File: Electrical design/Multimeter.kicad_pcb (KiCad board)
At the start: 2 copper layers, 191.5 x 133 mm, 191 parts, among them P101 CONN_02X07, P102 CONN_01X06, P201 10 A, P202 mA, P203 V R, P204 COMMON, P401 CONN_01X01, P402 CONN_01X01, P403 CONN_01X01, P404 CONN_01X01, P405 CONN_01X01, P406 CONN_01X05, P407 CONN_01X05, P501 USB_OTG, Q101 Q_PMOS_GSD, Q102 Q_NMOS_GSD, Q201 Q_NMOS_GSD, Q301 Q_PMOS_GSD, Q302 Q_NMOS_GSD, Q501 Q_NMOS_GSD, Q502 Q_PMOS_GSD, SW401 SW_PUSH, U101 STM32F373R8Tx, U102 ILI9341_LCD_Breakout, U103 BD4835, U201 CT138, U202 MCP6002, U203 MCP6N11, U204 74LVC1G66 GNDA, U205 CT138, U206 74LVC1G66 GNDA, U207 TSV634, U208 74LVC1G66 GNDA, U209 74LVC1G66 GNDA, U210 74LVC1G66 GNDA, U211 74LVC1G66 GNDA, U212 74LVC1G66 GNDA, U213 74LVC1G66 GNDA, U214 74LVC1G66 GNDA, U215 74LVC1G66 GNDA, U216 74LVC1G66 GNDA, U217 74LVC1G66 GNDA, U218 74LVC1G66 GNDA, U301 NCV551SN33T1G, U302 MAX6070, U501 TPD2E001, U502 MCP73834, Y101 8 MHz

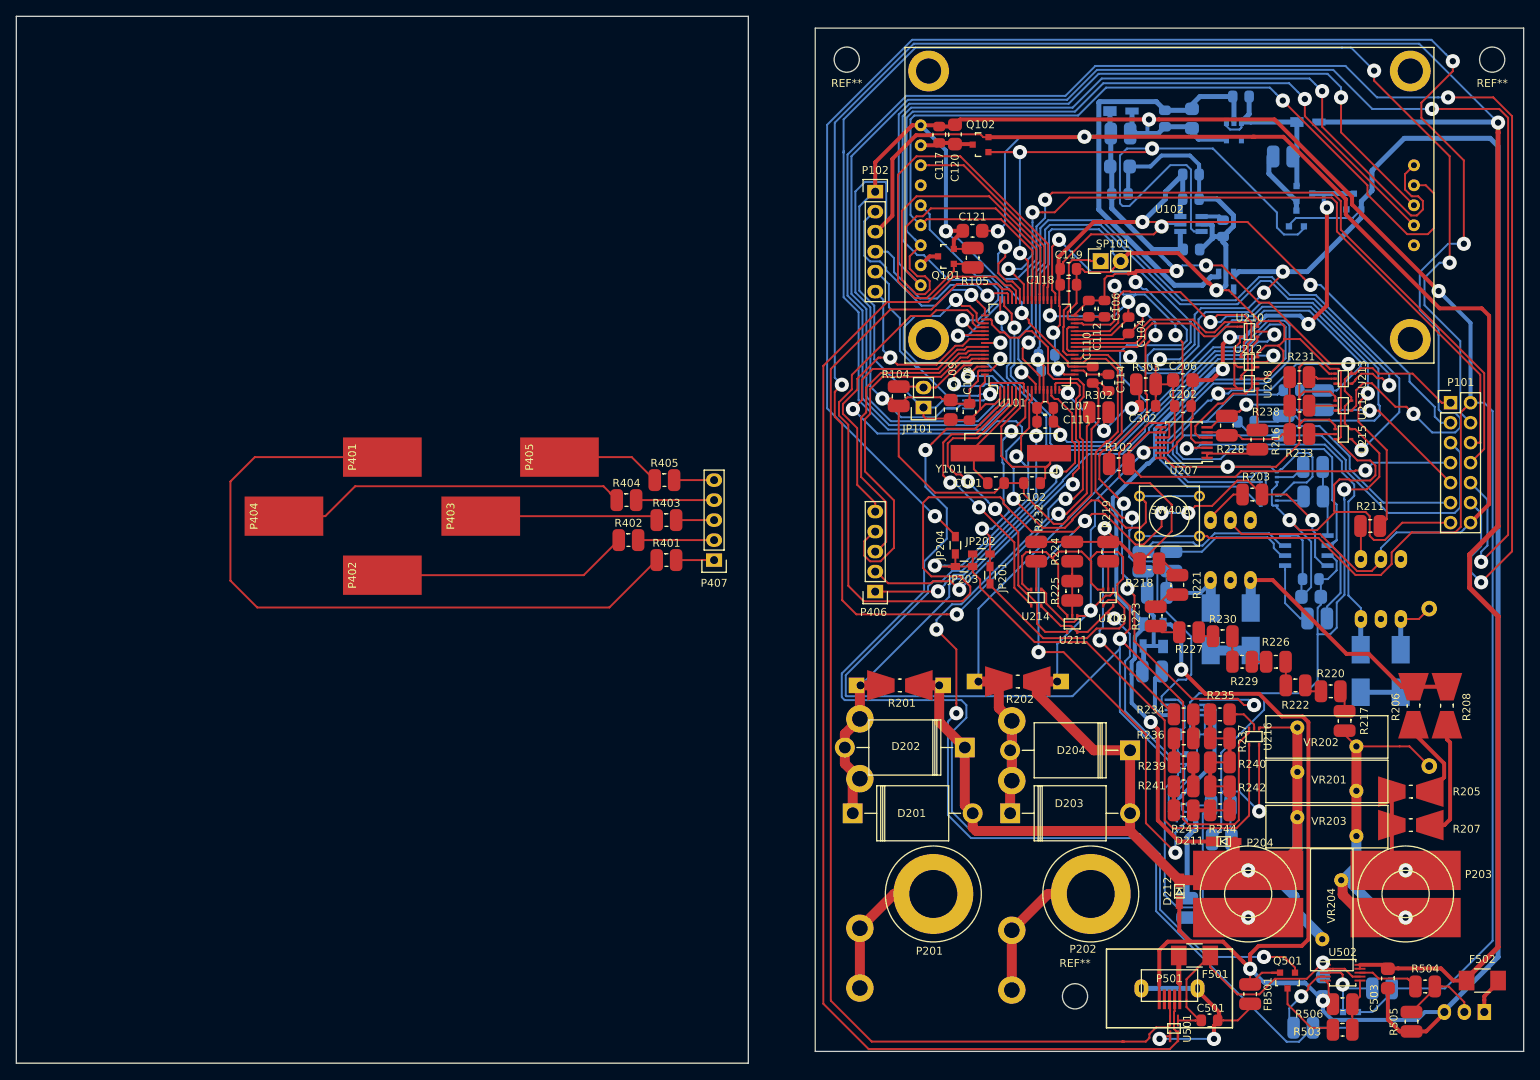
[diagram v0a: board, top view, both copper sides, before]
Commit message: Tied ground nets together, fixed clearance issues, added copper pours / zones.
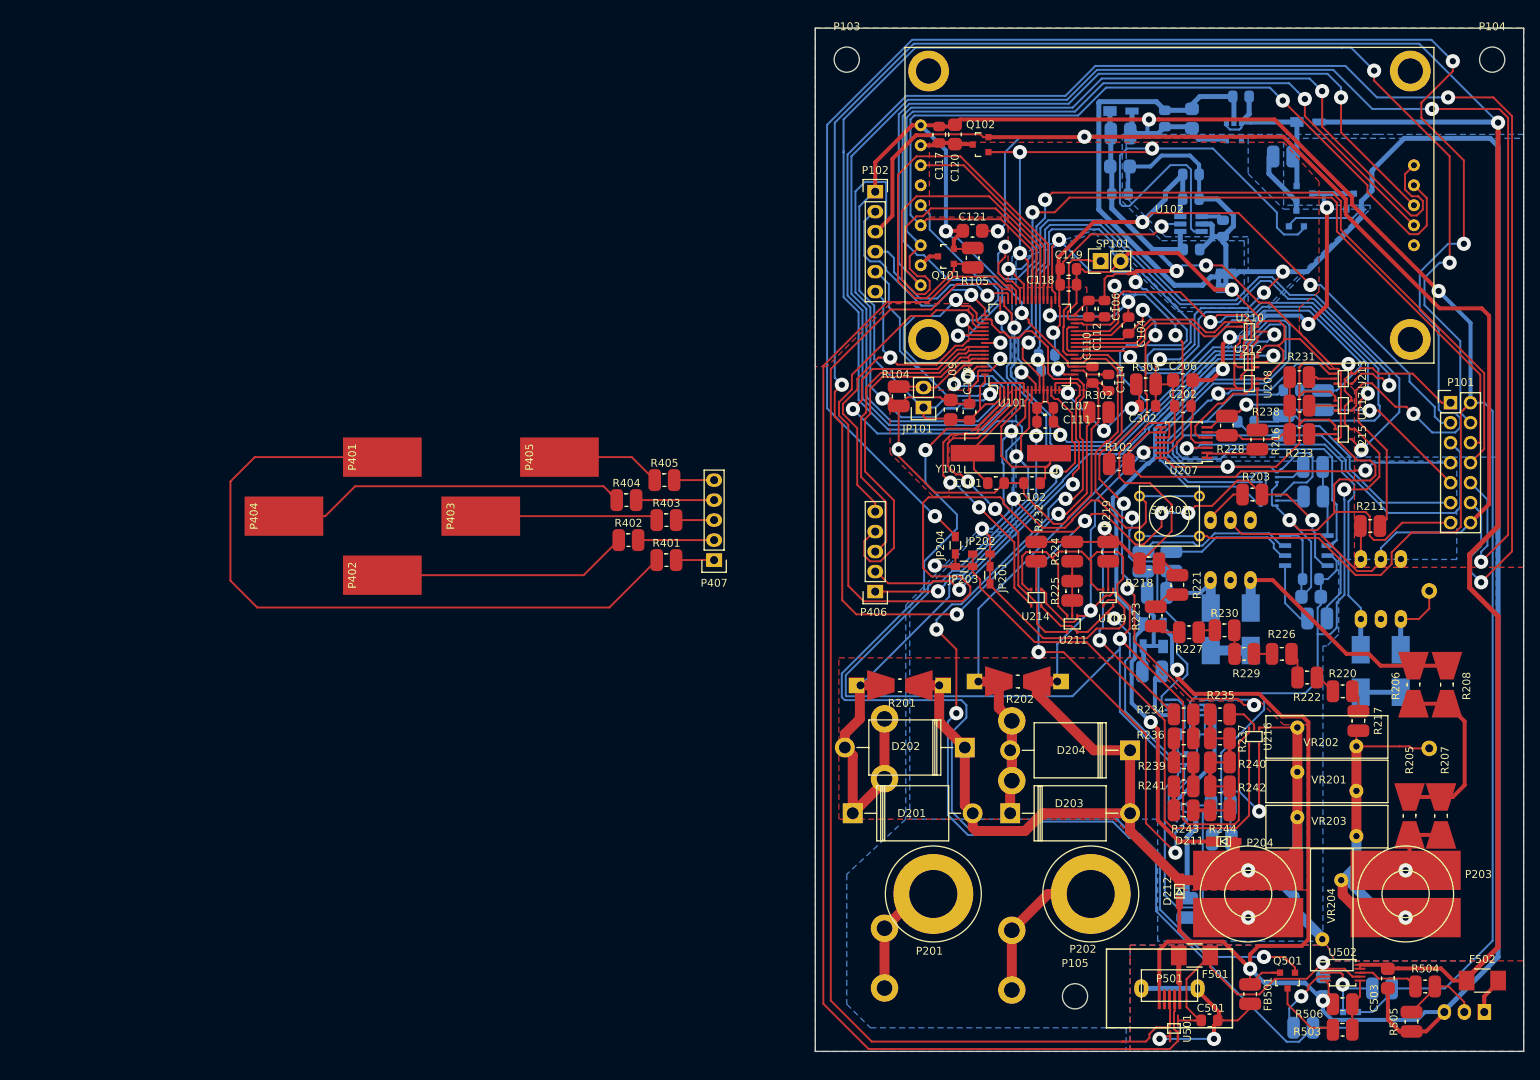
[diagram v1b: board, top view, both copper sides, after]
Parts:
- removed REF** (x3): MountingHole_3.2mm_M3, Mounting_Holes:MountingHole_3.2mm_M3
- added P103: Mounting hole, Mounting_Holes:MountingHole_3.2mm_M3, F.Cu at (144.0, 30.0)
- added P104: Mounting hole, Mounting_Holes:MountingHole_3.2mm_M3, F.Cu at (226.0, 30.0)
- added P105: Mounting hole, Mounting_Holes:MountingHole_3.2mm_M3, F.Cu at (173.0, 149.0)
- JP301, JP302: footprint Resistors_SMD:R_0805 -> my footprints:Net_Tie
- moved R207 4.01 mm to (219.5, 126.1), turned to 270 degrees
- moved F201 3.13 mm to (148.8, 130.9)
- moved R205 3.09 mm to (215.5, 126.1), turned to 270 degrees
- moved R206 2.67 mm to (216.0, 109.4)
- moved R208 2.67 mm to (220.2, 109.4)
- moved R215 2.25 mm to (218.0, 97.5)
- moved R222 1.79 mm to (202.5, 108.5)
- moved R217 1.75 mm to (209.0, 114.0)
- moved R220 1.52 mm to (207.0, 110.2)
- moved R226 1.25 mm to (199.3, 105.5)
- moved R229 1.04 mm to (194.5, 105.5)
- moved R230 0.79 mm to (192.0, 102.5)
- moved JP302 0.18 mm to (192.2, 59.0), turned to 0 degrees
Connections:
- R207 pad 1: Net-(R207-Pad1) -> Net-(R205-Pad1)
- R208 pad 2: Net-(R207-Pad1) -> Net-(R205-Pad1)
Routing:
- net Net-(R207-Pad1): track 15.1 -> 0.00 mm
- net /Main Input / Output/15A_Sense: track 95.5 -> 108.4 mm
- net Net-(R205-Pad1): track 10.9 -> 23.2 mm
- net Net-(F201-Pad1): track 18.7 -> 15.6 mm
- net /500mA_CHARGE: track 139.1 -> 141.7 mm
- net Net-(U101-Pad40): track 120.7 -> 118.2 mm
- net Net-(D209-Pad1): track 8.14 -> 10.4 mm
- net Net-(P203-Pad1): track 10.7 -> 8.71 mm
- net GNDD: track 369.9 -> 371.8 mm, vias 4 -> 5
- net Net-(P203-Pad2): track 57.4 -> 55.9 mm
- net /USB/CHARGE_STAT: track 153.1 -> 154.5 mm
- net Net-(D207-Pad1): track 34.2 -> 33.1 mm
- net /2V_R: track 107.6 -> 106.6 mm
- net +Vref: track 113.2 -> 114.1 mm
- net /Main Input / Output/COM: track 221.5 -> 222.4 mm
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- added copper zone on F.Cu, net +3V3
- added copper zone on F.Cu, net +5V
- added copper zone on F.Cu, net /Main Input / Output/COM
- added copper zone on B.Cu, net GND
- added copper zone on B.Cu, net GNDA
- added copper zone on B.Cu, net GNDD
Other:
- board size 191.5 x 133 mm -> 90 x 130 mm

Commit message: Add documentation. Fix some issues found while writing it.
The issues fixed:
Change R245-246 to 1M.
Remove D211-212 and add D213-214.
Power the analog switches from +V_int.
Reconfigure range combination jumpers.
Remove "GND" net.
Correct values of C103-105, and add R106-108 (correcting values of R101-103).
Change +V_int around to be based of +3.3VA instead of +BATT, and clamp to 3.5 V.
Along with above, remove GND rail, mostly replacing with GNDA.
Update PCB for changes.
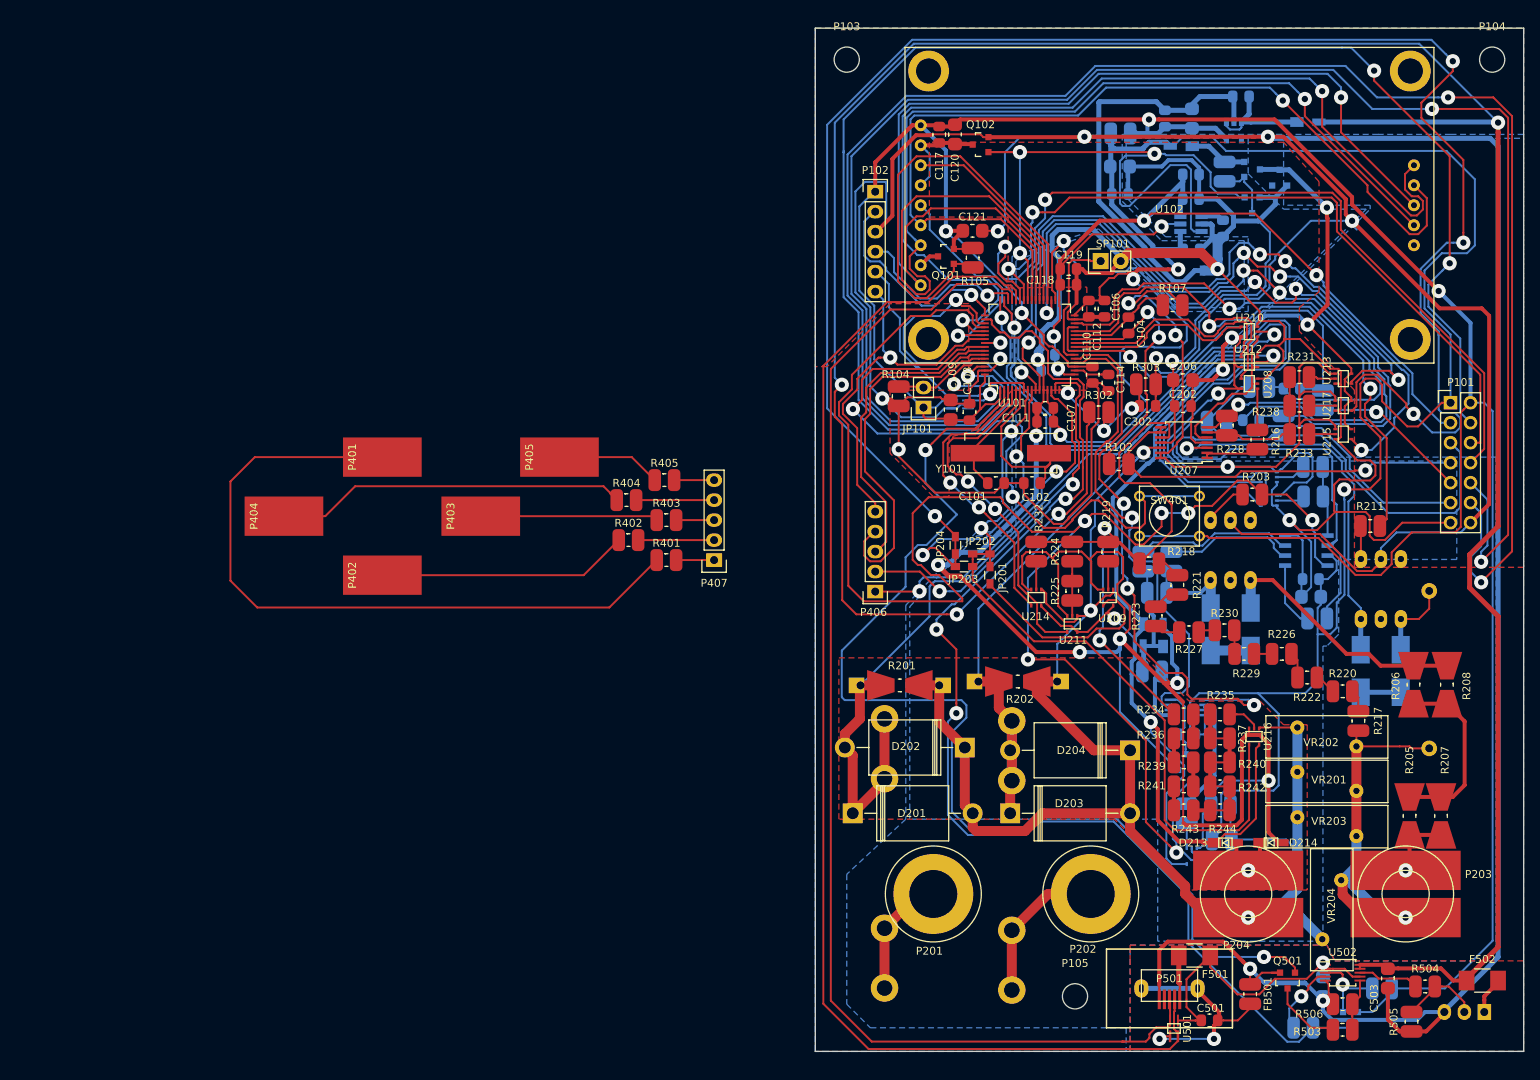
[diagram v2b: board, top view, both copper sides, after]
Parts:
- removed D211, D212: D_Schottky, my footprints:SC-90A
- removed JP301: JUMPER, my footprints:Net_Tie
- added D213: D_Schottky, my footprints:SC-90A, F.Cu at (192.1, 129.5)
- added D214: D_Schottky, my footprints:SC-90A, F.Cu at (197.9, 129.5)
- added R106: 500R, my footprints:SMDuniversal_0603to1210_HandSoldering, B.Cu at (191.0, 76.0)
- added R107: 500R, my footprints:SMDuniversal_0603to1210_HandSoldering, F.Cu at (185.4, 61.2)
- added R108: 500R, my footprints:SMDuniversal_0603to1210_HandSoldering, B.Cu at (196.4, 71.6)
- C103, C104, C105: value 0.22u -> 3.9n
- D301: value 4.7V -> 3.5V
- JP201, JP203: value Jumper_NC_Small -> Jumper_NO_Small
- JP202, JP204: value Jumper_NO_Small -> Jumper_NC_Small
- JP302: value JUMPER -> Net_Tie
- P101: value CONN_02X07 -> Expansion header
- P102: value CONN_01X06 -> Programming header
- R101, R102, R103: value 1k -> 500R
- R245, R246: value 100k -> 1M
- R247, R248: value 22R -> 68R
- moved R248 12.0 mm to (187.2, 125.8)
- moved D301 9.90 mm to (199.0, 45.0)
- moved D302 8.87 mm to (186.5, 41.0), turned to 180 degrees
- moved R301 7.66 mm to (192.0, 44.2), turned to 90 degrees
- moved Q301 7.31 mm to (195.5, 44.0)
- moved Q302 5.87 mm to (195.5, 48.5), turned to 0 degrees
- moved U218 5.69 mm to (187.8, 131.2)
- moved JP302 3.02 mm to (190.2, 56.8)
- moved C105 0.66 mm to (195.4, 75.8)
- moved C103 0.20 mm to (200.5, 71.8)
- turned P204 to 180 degrees
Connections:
- BT501 pad 3: GND -> GNDD
- C103 pad 2: /COMMON -> /COMMON_LV
- C104 pad 2: /COMMON -> /COMMON_V
- C105 pad 2: /COMMON -> /COMMON_Io
- C202 pad 2: GND -> GNDA
- C206 pad 1: GND -> GNDA
- C302 pad 2: GND -> GNDD
- C502 pad 2: GND -> GNDD
- C503 pad 2: GND -> GNDD
- D206 pad 2: GND -> GNDA
- D301 pad 1: GND -> GNDA
- D302 pad 1: +3.3VA -> Net-(D302-Pad1)
- D302 pad 2: +3V3 -> +3.3VA
- FB501 pad 1: GND -> GNDD
- JP201 pad 1: /20V_R -> Net-(JP201-Pad1)
- JP202 pad 2: /2V_R -> /20V_R
- JP203 pad 1: /2V_R -> /20V_R
- JP204 pad 2: Net-(JP204-Pad2) -> /2V_R
- P101 pad 11: /COMMON -> /Main Input / Output/COMMON
- P204 pad 2: Net-(P204-Pad2) -> Net-(D213-Pad2)
- P501 pad 5: GND -> GNDD
- Q301 pad 2: Net-(C301-Pad1) -> Net-(D302-Pad1)
- Q302 pad 2: GND -> GNDA
- Q501 pad 2: GND -> GNDD
- R248 pad 2: Net-(P204-Pad2) -> Net-(R248-Pad2)
- R301 pad 2: Net-(C301-Pad1) -> Net-(D302-Pad1)
- R303 pad 2: GND -> GNDD
- R505 pad 2: GND -> GNDD
- R506 pad 1: GND -> GNDD
- U101 pad 27: /COMMON -> /COMMON_V
- U101 pad 30: /COMMON -> /COMMON_LV
- U101 pad 35: /COMMON -> /COMMON_Io
- U102 pad 4: Net-(U102-Pad4) -> Net-(C117-Pad2)
- U202 pad 6: Net-(U202-Pad6) -> Net-(R248-Pad1)
- U202 pad 7: Net-(U202-Pad6) -> Net-(R248-Pad1)
- U204 pad 1: /COMMON -> /Main Input / Output/COMMON
- U204 pad 5: +3.3VA -> +V_int
- U206 pad 1: /COMMON -> /Main Input / Output/COMMON
- U206 pad 5: +3.3VA -> +V_int
- U207 pad 11: GND -> GNDA
- U207 pad 13: /COMMON -> /Main Input / Output/COMMON
- U207 pad 14: /COMMON -> /Main Input / Output/COMMON
- U208 pad 5: +3.3VA -> +V_int
- U209 pad 4: /20V_R -> Net-(JP201-Pad1)
- U209 pad 5: +3.3VA -> +V_int
- U210 pad 5: +3.3VA -> +V_int
- U211 pad 5: +3.3VA -> +V_int
- U212 pad 5: +3.3VA -> +V_int
- U213 pad 1: /COMMON -> /Main Input / Output/COMMON
- U213 pad 5: +3.3VA -> +V_int
- U214 pad 5: +3.3VA -> +V_int
- U215 pad 1: /COMMON -> /Main Input / Output/COMMON
- U215 pad 5: +3.3VA -> +V_int
- U216 pad 4: /2V_R -> /20V_R
- U216 pad 5: +3.3VA -> +V_int
- U217 pad 1: /COMMON -> /Main Input / Output/COMMON
- U217 pad 4: Net-(JP204-Pad2) -> /2V_R
- U217 pad 5: +3.3VA -> +V_int
- U218 pad 1: Net-(U202-Pad6) -> Net-(R248-Pad2)
- U218 pad 2: Net-(R248-Pad1) -> Net-(D213-Pad2)
- U218 pad 5: +3.3VA -> +V_int
- U502 pad 5: GND -> GNDD
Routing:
- net GND: track 362.3 -> 0.00 mm, vias 6 -> 0
- net GNDD: track 371.8 -> 639.7 mm, vias 5 -> 10
- net Net-(JP204-Pad2): track 220.8 -> 0.00 mm, vias 4 -> 0
- net /COMMON: track 192.8 -> 0.00 mm, vias 5 -> 0
- net /Main Input / Output/COMMON: track 0.00 -> 160.2 mm, vias 0 -> 3
- net /2V_R: track 106.6 -> 262.7 mm, vias 2 -> 6
- net +V_int: track 128.6 -> 247.0 mm, vias 5 -> 7
- net /COMMON_Io: track 0.00 -> 95.8 mm, vias 0 -> 3
- net /COMMON_LV: track 0.00 -> 66.0 mm, vias 0 -> 1
- net +3.3VA: track 368.7 -> 306.0 mm, vias 9 -> 4
- net /20V_R: track 55.8 -> 98.7 mm
- net GNDA: track 460.1 -> 492.4 mm, vias 5 -> 10
- net Net-(JP201-Pad1): track 0.00 -> 26.1 mm
- net /Main Input / Output/COM: track 222.4 -> 200.4 mm
- net Net-(D213-Pad2): track 0.00 -> 20.3 mm, vias 0 -> 1
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- removed copper zone on B.Cu, net GND

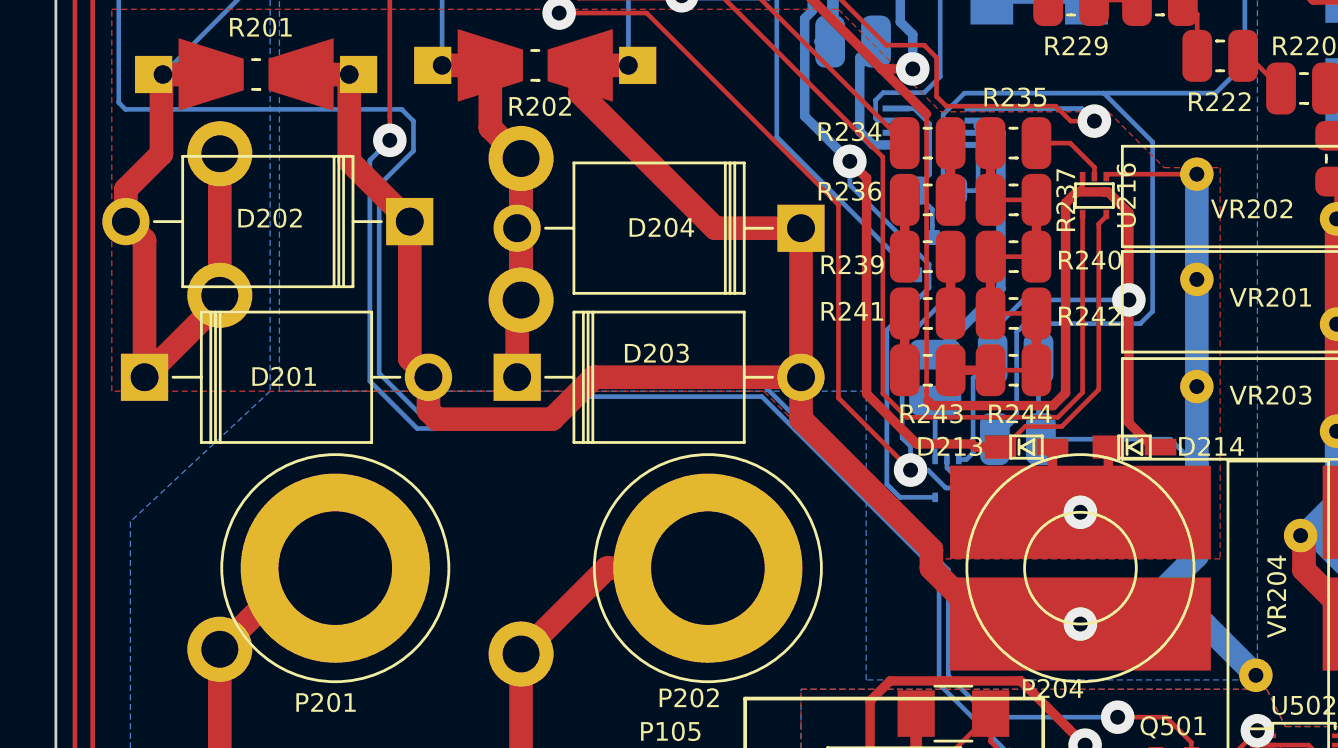
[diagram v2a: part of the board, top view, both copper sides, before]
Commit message: Added a resistor in COM to ensure clamping currents are handled correctly.
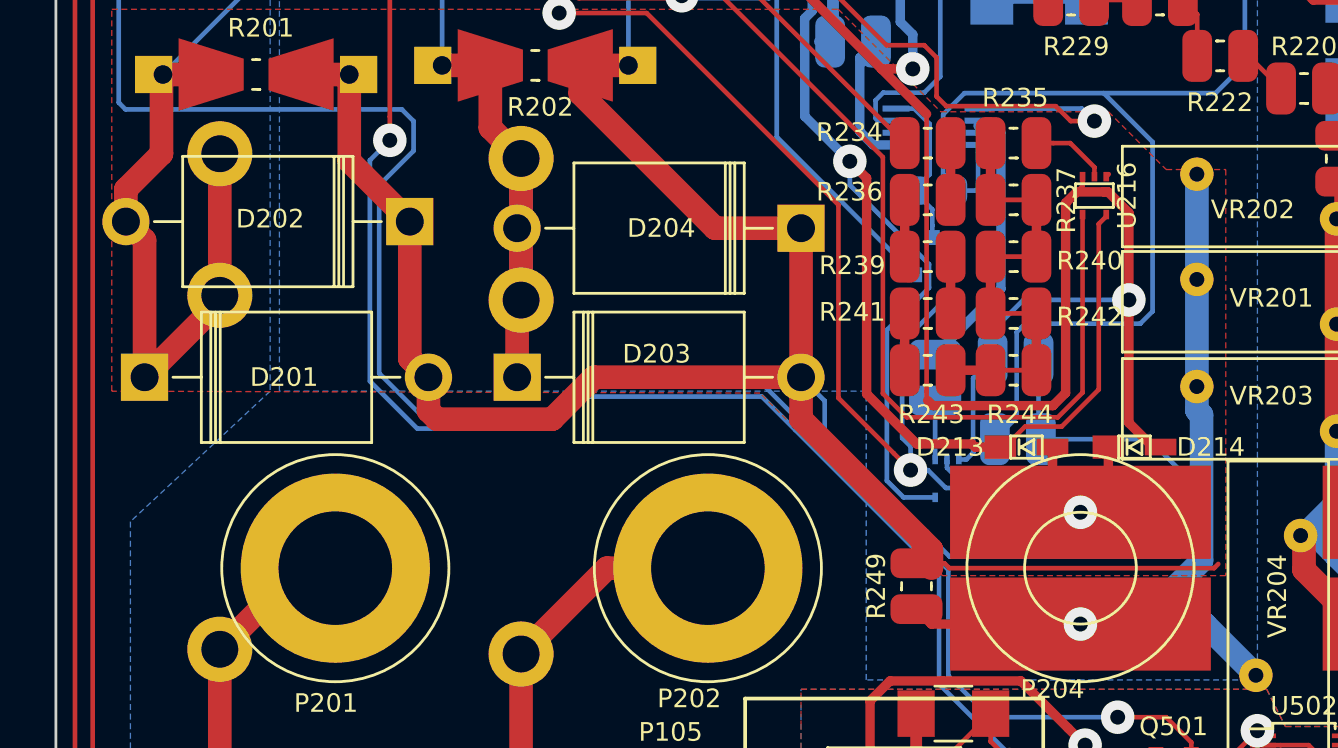
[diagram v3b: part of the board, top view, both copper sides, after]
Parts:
- added R249: 68R, my footprints:SMDuniversal_0603to1210_HandSoldering, F.Cu at (186.2, 137.0)
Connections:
- P204 pad 1: /Main Input / Output/COM -> Net-(P204-Pad1)
- VR201 pad 2: /Main Input / Output/COM -> Net-(P204-Pad1)
- VR202 pad 2: /Main Input / Output/COM -> Net-(P204-Pad1)
- VR203 pad 2: /Main Input / Output/COM -> Net-(P204-Pad1)
- VR204 pad 2: /Main Input / Output/COM -> Net-(P204-Pad1)
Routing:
- net Net-(P204-Pad1): track 0.00 -> 53.5 mm, vias 0 -> 1
- net /Main Input / Output/COM: track 200.4 -> 194.6 mm, vias 3 -> 2
